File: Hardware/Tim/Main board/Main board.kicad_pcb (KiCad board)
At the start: 4 copper layers, 175.3 x 104.1 mm, 168 parts, among them J1 SOICbite, J10 Conn_01x03_Socket, J11 Nichrome, J12 USB_C_Receptacle_USB2.0, J13 Conn_01x02_Socket, J14 Conn_01x02_Pin, J16 Conn_01x02_Pin, J2 USB_C_Receptacle_USB2.0, J3 Conn_01x04_Socket, J4 Conn_01x04_Socket, J5 Conn_01x04_Socket, J7 Conn_01x02_Socket, J8 U.FL, J9 SOICbite, Q1 IRLML0060TRPBF, Q2 IRLML0060TRPBF, U1 RP2040, U10 MAX-M10S, U11 ADP7105ACPZ-5.0-R7, U12 ADP7105ACPZ-3.3-R7, U13 ADP7105ACPZ-5.0-R7, U14 TPS2121RUXR, U15 TPS2121RUXR, U2 W25Q64JVZP, U3 MS5607-02BA, U4 BMI270, U5 ADP7105ACPZ-3.3-R7, U6 DRF1262TL, U7 RP2040, U8 W25Q64JVZP, U9 LT3120JV-PBF, Y1 445I23D12M00000, Y3 445I23D12M00000

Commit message: Routing donish maybe
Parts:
- C57: value 1uF -> 10uF
- U9: footprint Extra Footprints:LQFN28_Rev0_ADI -> BPPlib:LQFN28_Rev0_ADI
- moved J13 114.0 mm to (94.5, 114.3), turned to 0 degrees
- moved R13 109.8 mm to (101.2, 105.9), turned to 180 degrees
- moved R14 108.1 mm to (101.2, 104.8), turned to 180 degrees
- moved U10 90.9 mm to (90.5, 102.6), turned to 180 degrees
- moved D3 90.6 mm to (98.0, 95.3), turned to 0 degrees
- moved J7 88.1 mm to (106.3, 114.2), turned to 0 degrees
- moved R12 84.6 mm to (94.0, 95.3), turned to 180 degrees
- moved R44 82.8 mm to (105.5, 110.2), turned to 0 degrees
- moved C57 77.9 mm to (88.1, 96.3), turned to 180 degrees
- moved BT1 73.7 mm to (89.3, 92.3), turned to -90 degrees
- moved J3 46.9 mm to (128.7, 114.2)
- moved J4 46.9 mm to (142.7, 114.2)
- moved J5 46.9 mm to (156.8, 114.2)
- moved C49 44.4 mm to (131.5, 60.1)
- moved C50 44.4 mm to (132.9, 66.6)
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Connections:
- C24 pad 1: +1V1 -> Net-(U7-VREG_VOUT)
- C25 pad 1: +1V1 -> Net-(U7-VREG_VOUT)
- C26 pad 1: +1V1 -> Net-(U7-VREG_VOUT)
- C3 pad 1: +1V1 -> Net-(U1-VREG_VOUT)
- C4 pad 1: +1V1 -> Net-(U1-VREG_VOUT)
- C5 pad 1: +1V1 -> Net-(U1-VREG_VOUT)
- J9 pad 2: /SWD -> /SWD_R
- J9 pad 3: /SWCLK -> /SWCLK_R
- U1 pad 23: +1V1 -> Net-(U1-VREG_VOUT)
- U1 pad 45: +1V1 -> Net-(U1-VREG_VOUT)
- U1 pad 50: +1V1 -> Net-(U1-VREG_VOUT)
- U4 pad 1: /SPIO_POCI -> /SPI0_POCI
- U4 pad 13: /SPIO_SCK -> /SPI0_SCK
- U4 pad 14: /SPIO_PICO -> /SPI0_PICO
- U7 pad 23: +1V1 -> Net-(U7-VREG_VOUT)
- U7 pad 24: /SWCLK -> /SWCLK_R
- U7 pad 25: /SWD -> /SWD_R
- U7 pad 45: +1V1 -> Net-(U7-VREG_VOUT)
- U7 pad 50: +1V1 -> Net-(U7-VREG_VOUT)
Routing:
- net /Ch.3B: track 0.00 -> 93.5 mm, vias 0 -> 1
- net /Ch.3A: track 0.00 -> 90.7 mm, vias 0 -> 1
- net /Ch.2B: track 0.00 -> 76.0 mm, vias 0 -> 1
- net /Ch.2A: track 0.00 -> 75.0 mm, vias 0 -> 1
- net /SW: track 0.00 -> 74.3 mm, vias 0 -> 2
- net /Ch.1A: track 0.00 -> 72.5 mm, vias 0 -> 2
- net /Ch.1B: track 0.00 -> 69.9 mm, vias 0 -> 1
- net /TXEN: track 1.66 -> 70.6 mm, vias 0 -> 2
- net GND: track 273.9 -> 342.4 mm, vias 16 -> 29
- net +3V3: track 80.0 -> 146.5 mm, vias 5 -> 16
- net /DIO1: track 0.00 -> 46.1 mm, vias 0 -> 2
- net +5V: track 16.7 -> 62.5 mm
- net /BUSY: track 0.00 -> 44.8 mm, vias 0 -> 2
- net /TIMEPULSE: track 0.00 -> 42.3 mm, vias 0 -> 2
- net /~{RST}: track 0.00 -> 41.0 mm, vias 0 -> 2
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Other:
- board size 175.3 x 104.1 mm -> 163.6 x 70.7 mm

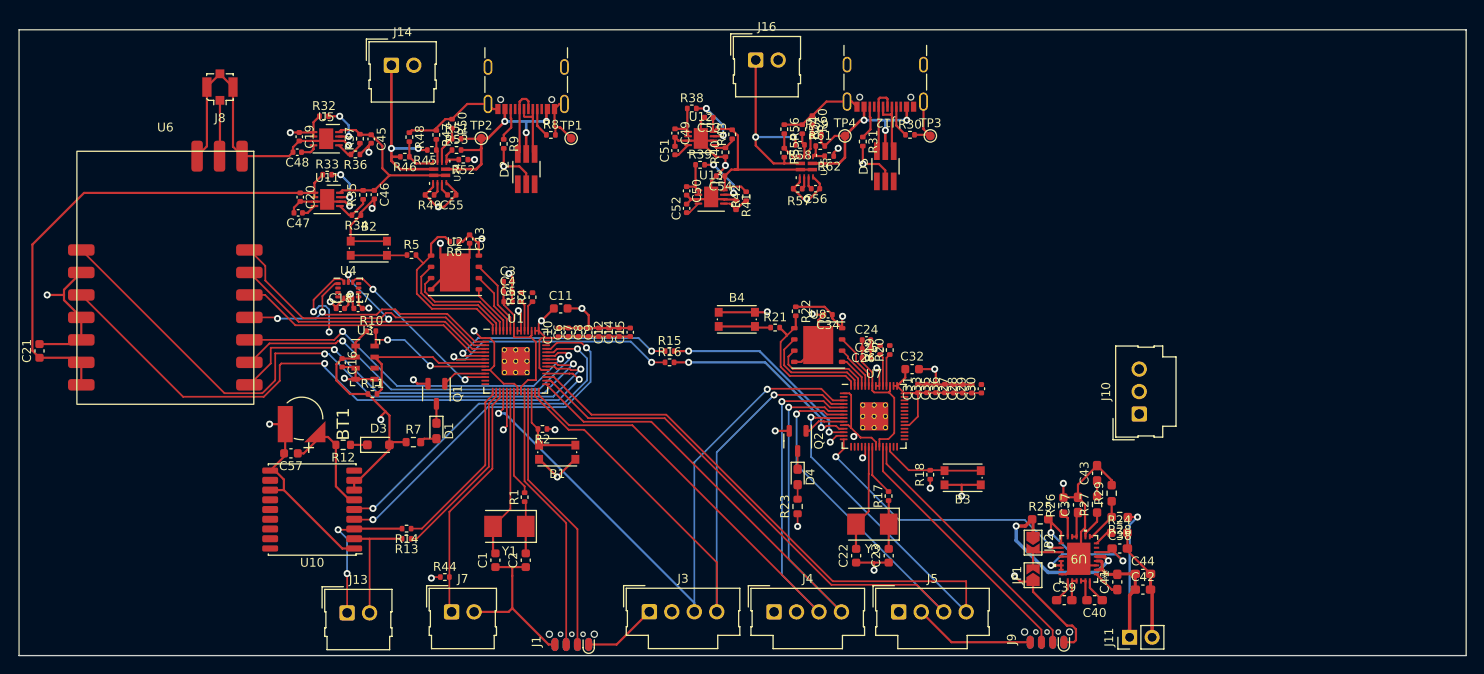
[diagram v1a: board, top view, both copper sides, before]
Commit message: Routing actually done and made smaller????
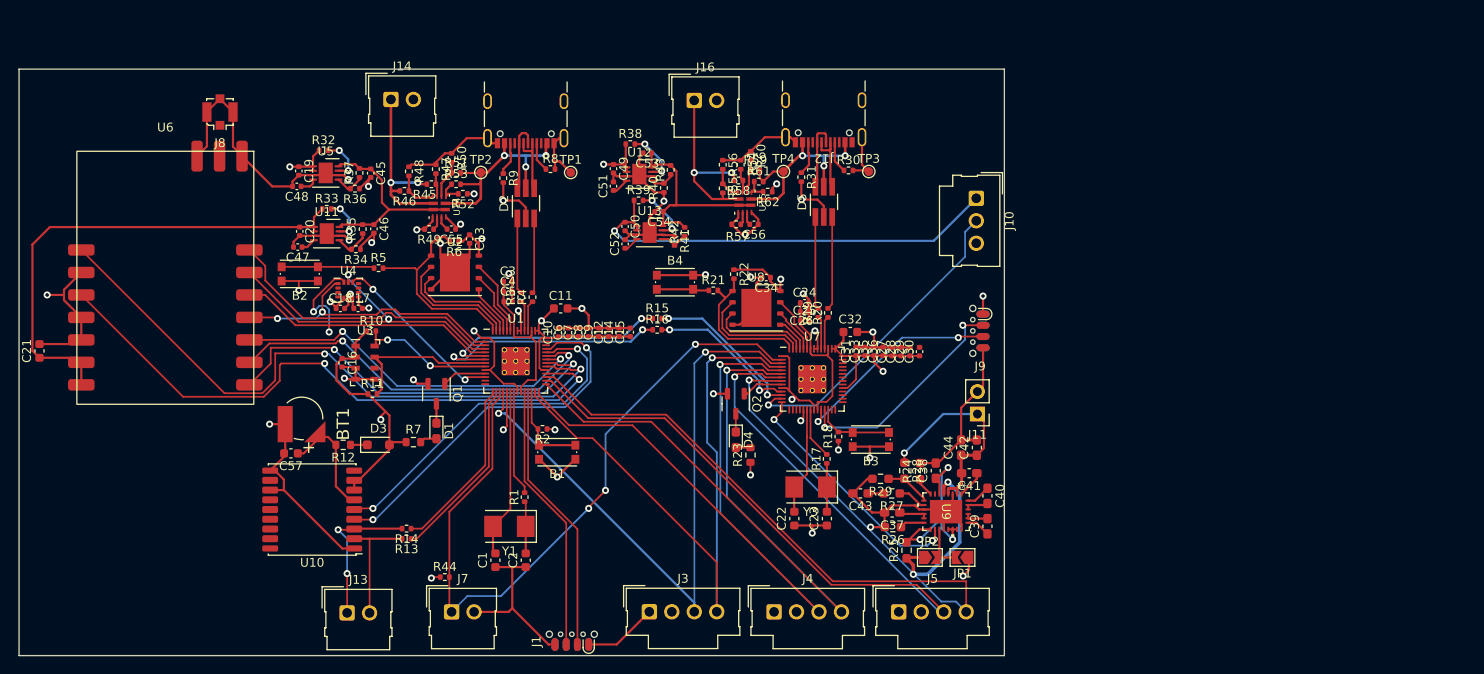
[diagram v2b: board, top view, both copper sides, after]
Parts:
- moved J9 36.5 mm to (167.1, 82.4), turned to 90 degrees
- moved J10 30.6 mm to (165.6, 67.4), turned to -90 degrees
- moved J11 30.5 mm to (165.7, 91.8), turned to 180 degrees
- moved C43 26.8 mm to (152.5, 100.8), turned to 180 degrees
- moved R29 26.2 mm to (154.8, 99.1), turned to 180 degrees
- moved C44 25.0 mm to (163.9, 95.6), turned to 90 degrees
- moved R28 24.9 mm to (157.5, 98.2), turned to -90 degrees
- moved C42 24.7 mm to (165.7, 95.6), turned to 90 degrees
- moved R24 23.6 mm to (159.2, 98.3), turned to 90 degrees
- moved R27 23.2 mm to (156.1, 100.8), turned to 180 degrees
- moved C38 22.6 mm to (161.0, 98.2), turned to 90 degrees
- moved C37 21.0 mm to (156.1, 103.0), turned to 180 degrees
- moved C41 20.8 mm to (164.8, 98.5), turned to 180 degrees
- moved R26 19.4 mm to (156.2, 104.6), turned to 180 degrees
- moved C40 16.9 mm to (166.9, 101.1), turned to -90 degrees
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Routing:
- net /LS1: track 27.4 -> 81.7 mm, vias 0 -> 3
- net +5V: track 62.5 -> 105.8 mm, vias 0 -> 1
- net /PWM_EMRG_REL: track 1.82 -> 35.6 mm
- net GND: track 342.4 -> 326.7 mm, vias 29 -> 32
- net /R_USB_D-: track 0.00 -> 10.5 mm
- net /R_USB_D+: track 0.00 -> 10.5 mm
- net /USB_D+: track 0.00 -> 8.57 mm
- net /USB_D-: track 0.00 -> 8.47 mm
- net /Ch.3B: track 93.5 -> 101.6 mm
- net /Ch.3A: track 90.7 -> 98.0 mm
- net /Ch.2B: track 76.0 -> 83.1 mm
- net /Ch.2A: track 75.0 -> 82.1 mm
- net Net-(J8-In): track 6.37 -> 0.11 mm
- net /CROSS_PRIMRX_REDTX: track 23.0 -> 17.2 mm
- net /CROSS_PRIMTX_REDRX: track 23.7 -> 17.9 mm
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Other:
- board size 163.6 x 70.7 mm -> 111.4 x 66.3 mm

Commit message: Adjusted/added things
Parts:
- added J15: Conn_01x04_Socket, Connector_Molex:Molex_SL_171971-0004_1x04_P2.54mm_Vertical, F.Cu at (62.7, 101.0)
- added J6: Conn_01x02_Socket, Connector_Molex:Molex_SL_171971-0002_1x02_P2.54mm_Vertical, F.Cu at (97.0, 114.3)
- added JP3: SolderJumper_2_Open, Jumper:SolderJumper-2_P1.3mm_Open_TrianglePad1.0x1.5mm, F.Cu at (70.9, 99.9)
- added JP4: SolderJumper_2_Open, Jumper:SolderJumper-2_P1.3mm_Open_TrianglePad1.0x1.5mm, F.Cu at (67.7, 99.9)
- added R63: 10k, Resistor_SMD:R_0402_1005Metric, F.Cu at (96.4, 110.5)
- moved J13 6.35 mm to (88.1, 114.3)
- moved C10 0.44 mm to (118.4, 82.2)
- moved C12 0.44 mm to (124.1, 82.1)
- moved C14 0.44 mm to (125.2, 82.1)
- moved C15 0.44 mm to (126.5, 82.1)
- moved C6 0.44 mm to (119.5, 82.1)
- moved C7 0.44 mm to (120.7, 82.1)
- moved C8 0.44 mm to (121.8, 82.1)
- moved C9 0.44 mm to (122.9, 82.1)
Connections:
- U1 pad 13: /PWM_ART -> /LS2
- U1 pad 36: /~{RST} -> /BUSY
- U1 pad 37: /BUSY -> /~{RST}
- U1 pad 40: unconnected-(U1-GPIO28_ADC2-Pad40) -> /STEP
- U1 pad 41: unconnected-(U1-GPIO29_ADC3-Pad41) -> /DIR
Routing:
- net /DIR: track 0.00 -> 106.0 mm, vias 0 -> 1
- net /STEP: track 0.00 -> 105.4 mm, vias 0 -> 1
- net /LS2: track 0.00 -> 37.4 mm, vias 0 -> 1
- net +5V: track 105.8 -> 117.8 mm
- net /~{RST}: track 41.0 -> 50.4 mm
- net Net-(J15-Pin_1): track 0.00 -> 8.29 mm
- net Net-(J13-Pin_2): track 13.8 -> 19.8 mm
- net /BUSY: track 44.8 -> 49.9 mm
- net /TIMEPULSE: track 42.3 -> 46.1 mm
- net /EXTINT: track 40.1 -> 43.6 mm
- net +3V3: track 141.4 -> 144.7 mm, vias 19 -> 21
- net /DIO1: track 46.1 -> 48.7 mm
- net Net-(J13-Pin_1): track 17.1 -> 19.0 mm
- net /TXEN: track 70.6 -> 69.3 mm

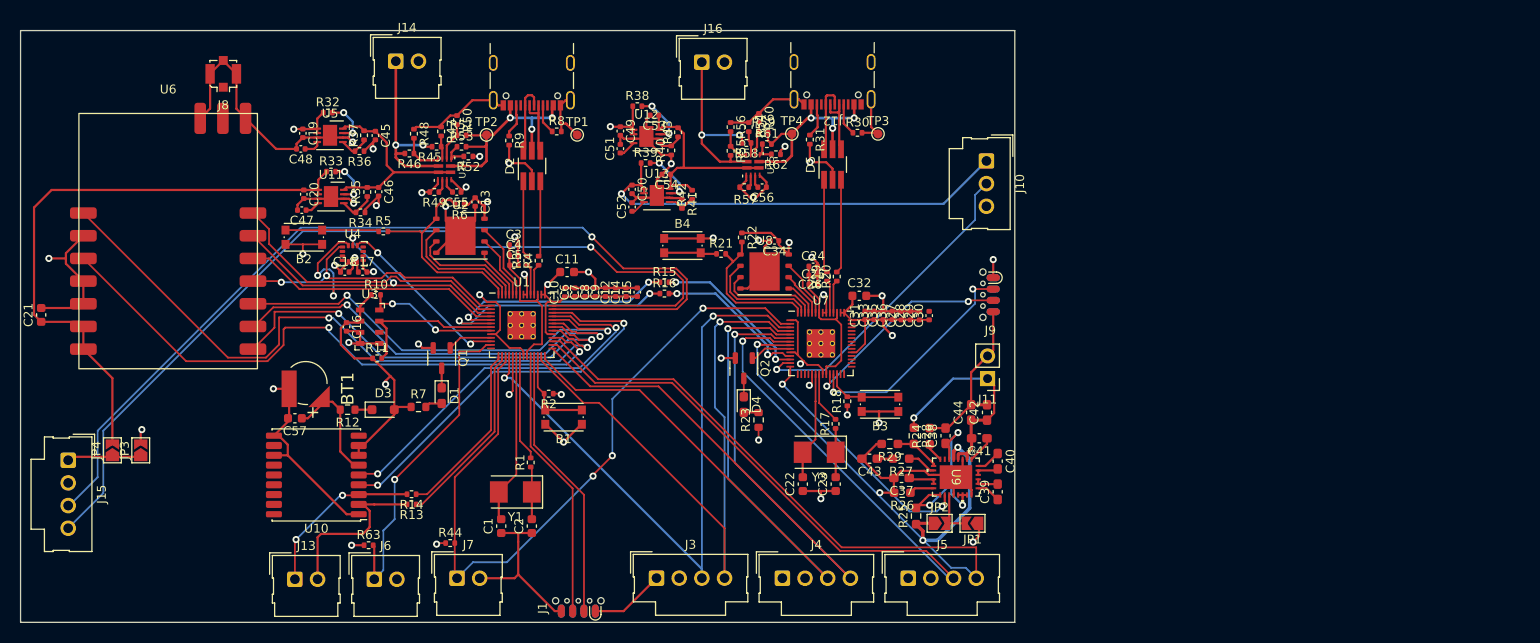
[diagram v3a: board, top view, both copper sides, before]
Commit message: Resistor size change
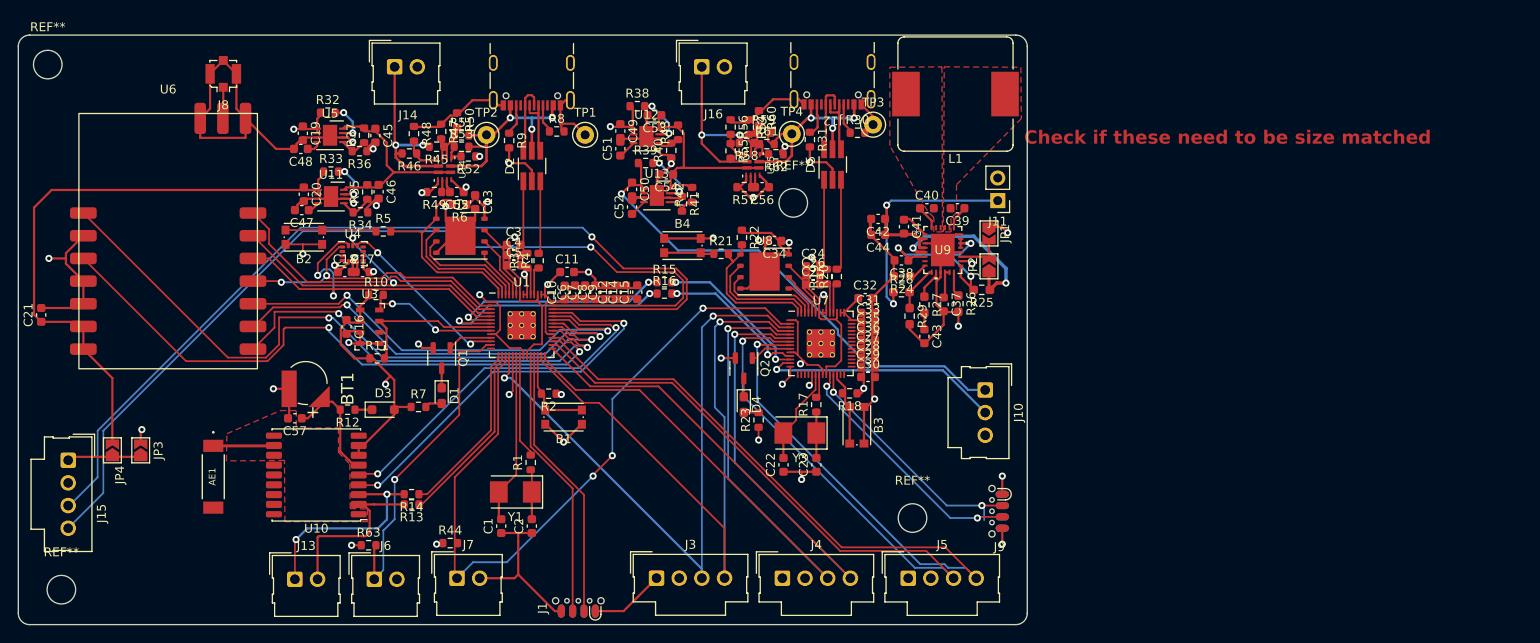
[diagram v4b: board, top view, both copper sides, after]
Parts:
- added AE1: Antenna, BPPlib:ANT_1575AT_JOT-M, F.Cu at (79.0, 102.8)
- added L1: 3.3uH, BPPlib:L_Bourns_SRP1265A, F.Cu at (162.1, 59.9)
- added REF**: MountingHole_3.2mm_M3, MountingHole:MountingHole_3.2mm_M3, F.Cu at (144.0, 72.1)
- added REF**: MountingHole_3.2mm_M3, MountingHole:MountingHole_3.2mm_M3, F.Cu at (60.5, 56.6)
- added REF**: MountingHole_3.2mm_M3, MountingHole:MountingHole_3.2mm_M3, F.Cu at (157.3, 107.4)
- added REF**: MountingHole_3.2mm_M3, MountingHole:MountingHole_3.2mm_M3, F.Cu at (62.0, 115.5)
- C10, C12, C13, C14, C15, C16, C17, C18, C19, C20, C24, C25, C26, C27, C28, C29, C3, C30, C31, C33, C34, C35, C36, C4, C45, C46, C47, C48, C49, C5, C50, C51, C52, C53, C54, C55, C56, C6, C7, C8, C9: footprint Capacitor_SMD:C_0402_1005Metric -> Capacitor_SMD:C_0603_1608Metric
- C37, C38, C39, C40, C41, C42, C43, C44: footprint Capacitor_SMD:C_0603_1608Metric_Pad1.08x0.95mm_HandSolder -> Capacitor_SMD:C_0603_1608Metric
- R1, R10, R11, R13, R14, R15, R16, R17, R18, R19, R2, R20, R21, R22, R3, R30, R31, R32, R33, R34, R35, R36, R37, R38, R39, R4, R40, R41, R42, R43, R44, R45, R46, R47, R48, R49, R5, R50, R51, R52, R53, R54, R55, R56, R57, R58, R59, R6, R60, R61, R62, R63, R8, R9: footprint Resistor_SMD:R_0402_1005Metric -> Resistor_SMD:R_0603_1608Metric
- TP1, TP2, TP3, TP4: footprint TestPoint:TestPoint_Pad_D1.0mm -> TestPoint:TestPoint_Keystone_5000-5004_Miniature
- moved JP1 32.5 mm to (165.9, 75.6), turned to -90 degrees
- moved C39 32.1 mm to (162.4, 72.7), turned to 180 degrees
- moved C40 29.4 mm to (158.9, 72.7), turned to 0 degrees
- moved JP2 29.3 mm to (165.9, 79.2), turned to 90 degrees
- moved R25 26.4 mm to (165.1, 81.9), turned to 180 degrees
- moved J10 25.7 mm to (165.5, 93.1)
- moved U9 25.5 mm to (160.7, 77.4), turned to 0 degrees
- moved C41 25.2 mm to (156.4, 74.8), turned to -90 degrees
- moved C42 24.9 mm to (153.5, 73.9), turned to 180 degrees
- moved J9 24.3 mm to (168.1, 106.7)
- moved C44 22.5 mm to (153.5, 75.7), turned to 180 degrees
- moved R26 22.1 mm to (162.5, 83.4), turned to -90 degrees
- moved C38 20.3 mm to (156.1, 78.6), turned to 180 degrees
- moved C37 20.0 mm to (160.8, 83.5), turned to -90 degrees
- moved J11 20.0 mm to (166.9, 71.9)
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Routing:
- net /CUT: track 27.8 -> 3.73 mm
- net GND: track 326.2 -> 314.8 mm
- net Net-(J11-Pin_1): track 24.4 -> 34.9 mm, vias 1 -> 2
- net /PWM_EMRG_REL: track 35.6 -> 27.3 mm
- net Net-(AE1-A): track 0.00 -> 6.81 mm
- net +5V: track 117.8 -> 124.6 mm
- net Net-(J13-Pin_1): track 19.0 -> 24.0 mm
- net /SWCLK_R: track 24.1 -> 27.9 mm
- net +3V3: track 144.7 -> 141.0 mm, vias 21 -> 20
- net Net-(J8-In): track 0.11 -> 3.55 mm
- net Net-(U7-XOUT): track 5.83 -> 3.05 mm
- net Net-(C39-Pad2): track 2.69 -> 0.00 mm
- net Net-(C40-Pad2): track 2.75 -> 0.24 mm
- net /SWD_R: track 26.0 -> 27.9 mm
- net /Ch.3A: track 98.0 -> 99.6 mm
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- added copper zone on F.Cu, net GND
- added copper zone on F.Cu, net Net-(C39-Pad2)
- added copper zone on F.Cu, net Net-(C40-Pad2)
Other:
- board size 111.4 x 66.3 mm -> 113 x 66 mm
- board text added: "Check if these need to be size matched"
